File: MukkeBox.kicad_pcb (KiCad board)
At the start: 2 copper layers, 175 x 105 mm, 295 parts, among them J1 TB001-500-06BE CUI_Devices, J101 Conn_02x20_Odd_Even, J103 Conn_02x05_Odd_Even, J104 Conn_02x01, J301 Conn_02x04_Odd_Even, J302 Conn_02x04_Odd_Even, J303 TB001-500-04BE CUI_Devices, J401 TB001-500-02BE CUI_Devices, J601 Conn_01x03_Female, J602 Conn_02x01, J603 Conn_02x06_Odd_Even, J604 Conn_02x01, J605 Conn_02x01, Q1 2N7002, Q201 VS6412AE, Q301 2N7002, Q302 HSBB3103, Q303 2N7002, Q304 HSBB3103, Q305 VS6412AE, Q306 2N7002, Q307 BSS84, Q308 2N7002, Q309 VS6412AE, Q310 HSBB3103, Q311 HSBB3103, Q501 2N7002, U1 TPA3116D2, U102 STM32F030C6Tx_MukkeBox, U103 MCP9700, U2 TPA3116D2, U203 TPS40210, U301 BQ24610, U502 BK8000L, U503 TDA7719, U504 AP2553AW6-7, U505 JW5026, U602 JW5026, Y101 FOXSDLF/080-20

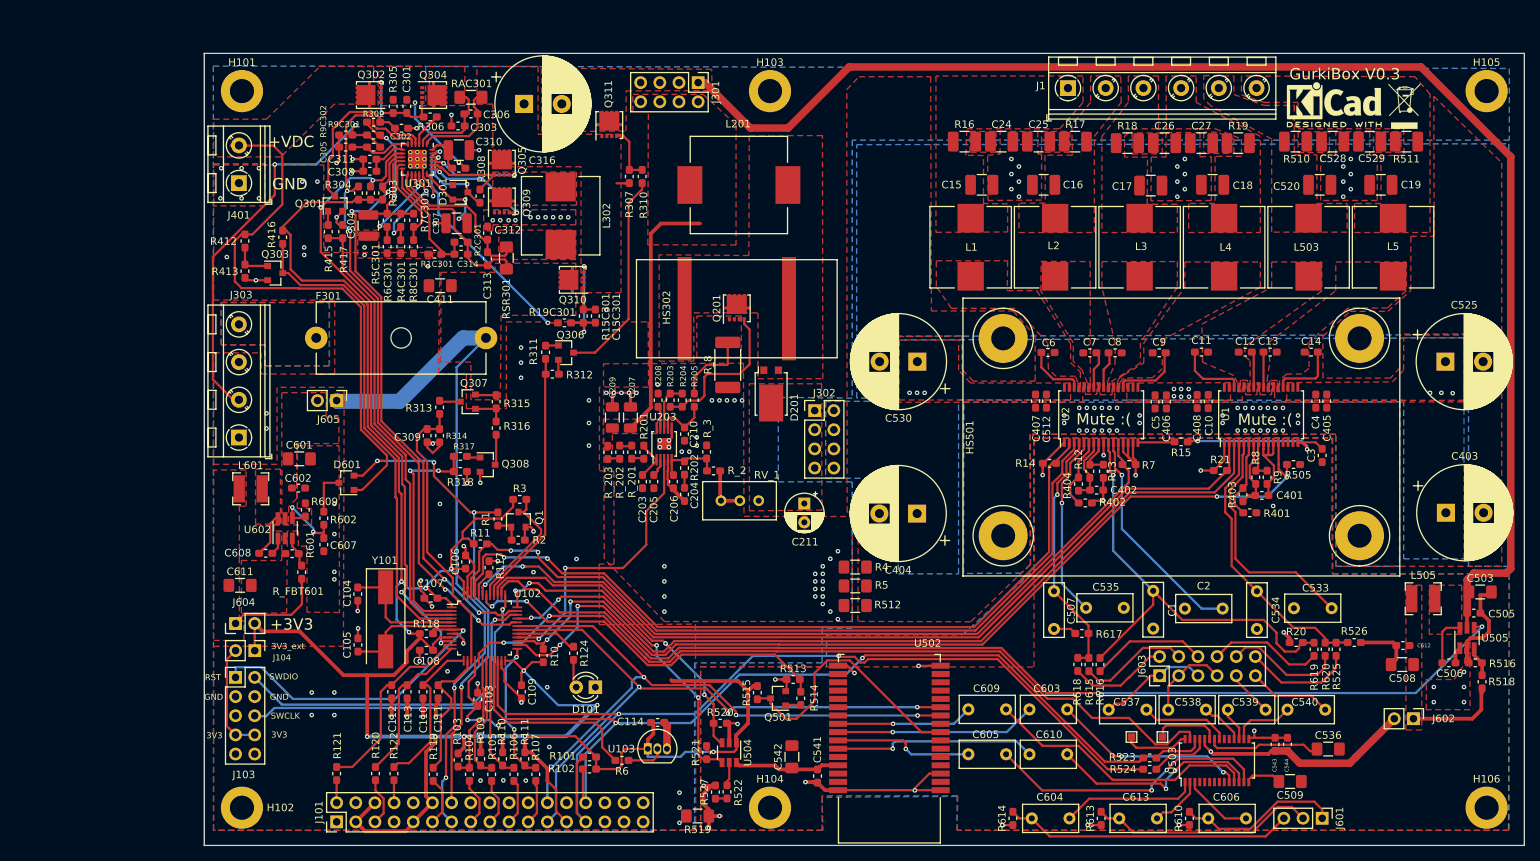
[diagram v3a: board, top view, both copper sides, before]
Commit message: MukkePlatine auf EuroPlatinen groesse geändert
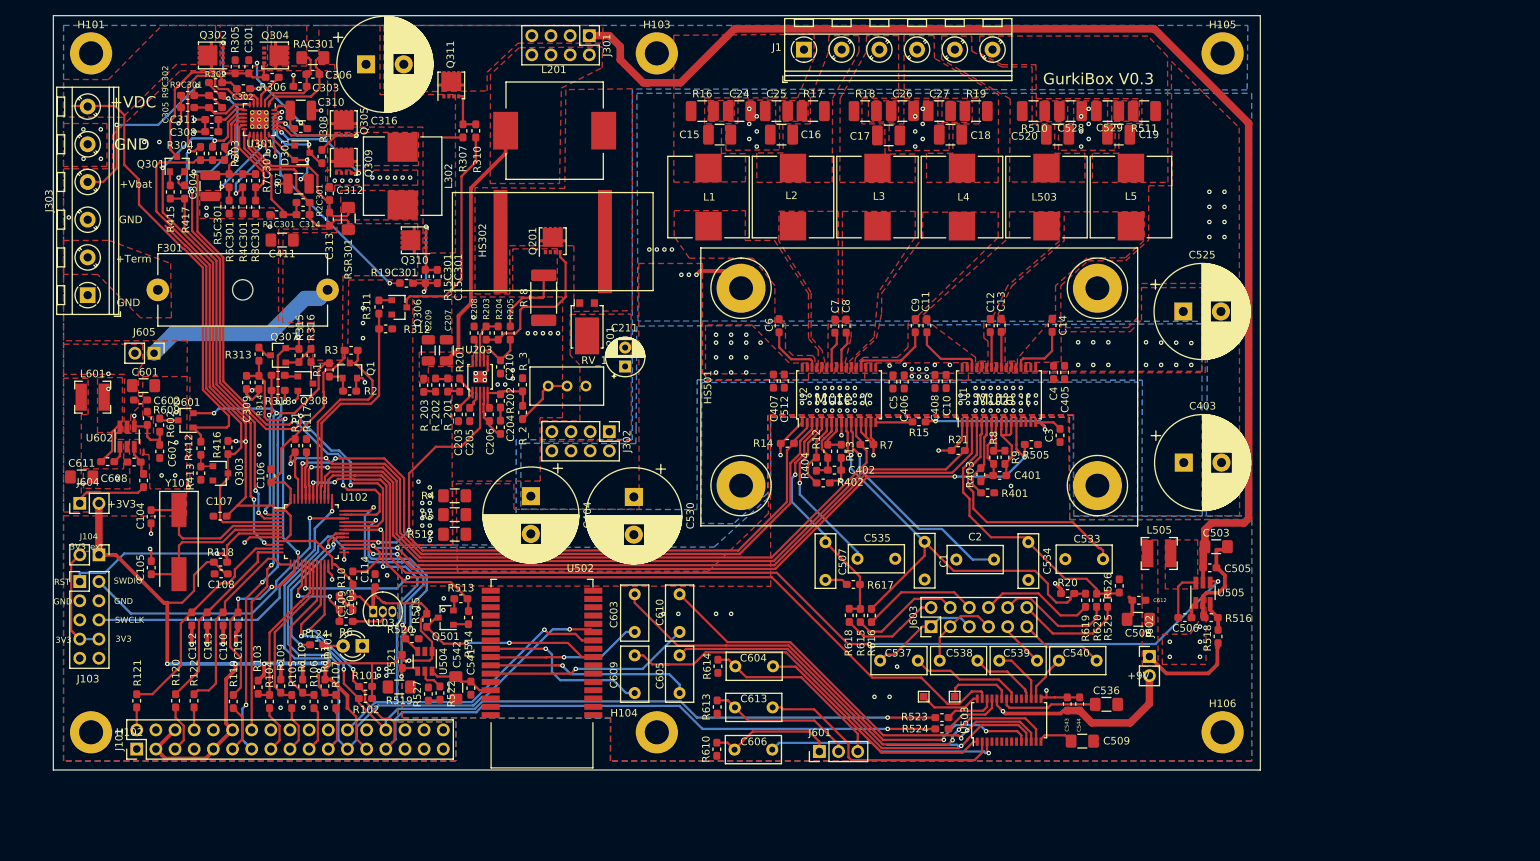
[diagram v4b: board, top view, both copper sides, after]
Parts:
- removed J401: TB001-500-02BE CUI_Devices, TerminalBlock_RND:TerminalBlock_RND_205-00045_1x02_P5.00mm_Horizontal
- removed REF**: WEEE-Logo_4.2x6mm_SilkScreen, Symbol:WEEE-Logo_4.2x6mm_SilkScreen
- removed REF**: KiCad-Logo2_5mm_SilkScreen, Symbol:KiCad-Logo2_5mm_SilkScreen
- J303: value TB001-500-04BE CUI_Devices -> TB001-500-06BE CUI_Devices; footprint TerminalBlock_RND:TerminalBlock_RND_205-00047_1x04_P5.00mm_Horizontal -> TerminalBlock_RND:TerminalBlock_RND_205-00049_1x06_P5.00mm_Horizontal
- moved J601 67.2 mm to (152.0, 129.6), turned to 90 degrees
- moved C606 63.5 mm to (145.8, 129.4)
- moved R610 63.3 mm to (138.4, 129.3)
- moved C603 59.3 mm to (127.5, 108.8), turned to 270 degrees
- moved R4 53.9 mm to (103.7, 95.7)
- moved R5 53.9 mm to (103.7, 98.2)
- moved R512 53.9 mm to (103.7, 100.8)
- moved C613 53.0 mm to (145.8, 123.8)
- moved R613 53.0 mm to (138.5, 123.7)
- moved C404 51.3 mm to (113.8, 95.8), turned to 270 degrees
- moved C610 49.1 mm to (133.5, 113.8), turned to 90 degrees
- moved C541 47.4 mm to (105.8, 121.2)
- moved U502 47.1 mm to (115.2, 119.3)
- moved C542 45.5 mm to (103.8, 121.2), turned to 270 degrees
- moved Q501 45.3 mm to (102.5, 111.9)
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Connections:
- D301 pad 1: (no net) -> Net-(D301-Pad1)
- J101 pad 29: (no net) -> Net-(J101-Pad29)
- J101 pad 30: (no net) -> Net-(J101-Pad30)
- J101 pad 31: (no net) -> Net-(J101-Pad31)
- J101 pad 32: (no net) -> Net-(J101-Pad32)
- J101 pad 33: (no net) -> Net-(J101-Pad33)
- J101 pad 34: (no net) -> Net-(J101-Pad34)
- J103 pad 10: (no net) -> Net-(J103-Pad10)
- J103 pad 5: (no net) -> Net-(J103-Pad5)
- J103 pad 9: (no net) -> Net-(J103-Pad9)
- J303 pad 2: /00_Charger/TS -> Net-(F301-Pad1)
- J303 pad 4: Net-(F301-Pad1) -> /00_Charger/TS
- U502 pad 12: (no net) -> Net-(U502-Pad12)
- U502 pad 13: (no net) -> Net-(U502-Pad13)
- U502 pad 14: (no net) -> Net-(U502-Pad14)
- U502 pad 15: (no net) -> Net-(U502-Pad15)
- U502 pad 18: (no net) -> Net-(U502-Pad18)
- U502 pad 19: (no net) -> Net-(U502-Pad19)
- U502 pad 2: (no net) -> Net-(U502-Pad2)
- U502 pad 20: (no net) -> Net-(U502-Pad20)
- U502 pad 21: (no net) -> Net-(U502-Pad21)
- U502 pad 22: (no net) -> Net-(U502-Pad22)
- U502 pad 23: (no net) -> Net-(U502-Pad23)
- U502 pad 28: (no net) -> Net-(U502-Pad28)
- U502 pad 30: (no net) -> Net-(U502-Pad30)
- U502 pad 31: (no net) -> Net-(U502-Pad31)
- U502 pad 4: (no net) -> Net-(U502-Pad4)
- U502 pad 5: (no net) -> Net-(U502-Pad5)
- U502 pad 6: (no net) -> Net-(U502-Pad6)
- U502 pad 7: (no net) -> Net-(U502-Pad7)
- U502 pad 9: (no net) -> Net-(U502-Pad9)
- U503 pad 19: (no net) -> Net-(U503-Pad19)
- U503 pad 20: (no net) -> Net-(U503-Pad20)
- U503 pad 4: (no net) -> Net-(U503-Pad4)
- U503 pad 5: (no net) -> Net-(U503-Pad5)
- U503 pad 6: (no net) -> Net-(U503-Pad6)
- U503 pad 7: (no net) -> Net-(U503-Pad7)
- U503 pad 8: (no net) -> Net-(U503-Pad8)
- U503 pad 9: (no net) -> Net-(U503-Pad9)
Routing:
- net GNDA: track 112.3 -> 58.3 mm, vias 25 -> 24
- net +3V3: track 321.7 -> 269.8 mm, vias 13 -> 9
- net Net-(C603-Pad1): track 26.0 -> 62.4 mm
- net GND: track 93.2 -> 57.7 mm, vias 119 -> 88
- net Net-(C609-Pad2): track 36.5 -> 71.3 mm, vias 0 -> 1
- net Net-(C610-Pad2): track 28.6 -> 57.4 mm
- net Net-(C613-Pad1): track 7.26 -> 33.6 mm
- net /00_Charger/TS: track 55.4 -> 29.3 mm
- net Net-(C606-Pad1): track 9.27 -> 31.2 mm, vias 0 -> 1
- net MUTE_AMP2: track 126.2 -> 104.3 mm
- net SYSTEM_LOAD: track 185.9 -> 165.1 mm
- net /TEMP_SENSOR1: track 32.7 -> 12.4 mm
- net SDA: track 129.3 -> 109.7 mm, vias 2 -> 3
- net Net-(C605-Pad1): track 37.9 -> 56.9 mm
- net /GPIO4: track 18.7 -> 36.3 mm
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- removed copper zone on B.Cu, net Net-(F301-Pad1)
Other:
- board size 175 x 105 mm -> 160 x 100 mm
- board text added: "+9V"
- board text added: "+Term"
- board text added: "+Vbat"

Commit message: fertig zum bestellen
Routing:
- net Net-(Q201-Pad4): track 20.5 -> 19.4 mm
- net GNDA: vias 24 -> 37
- net GND: vias 88 -> 100

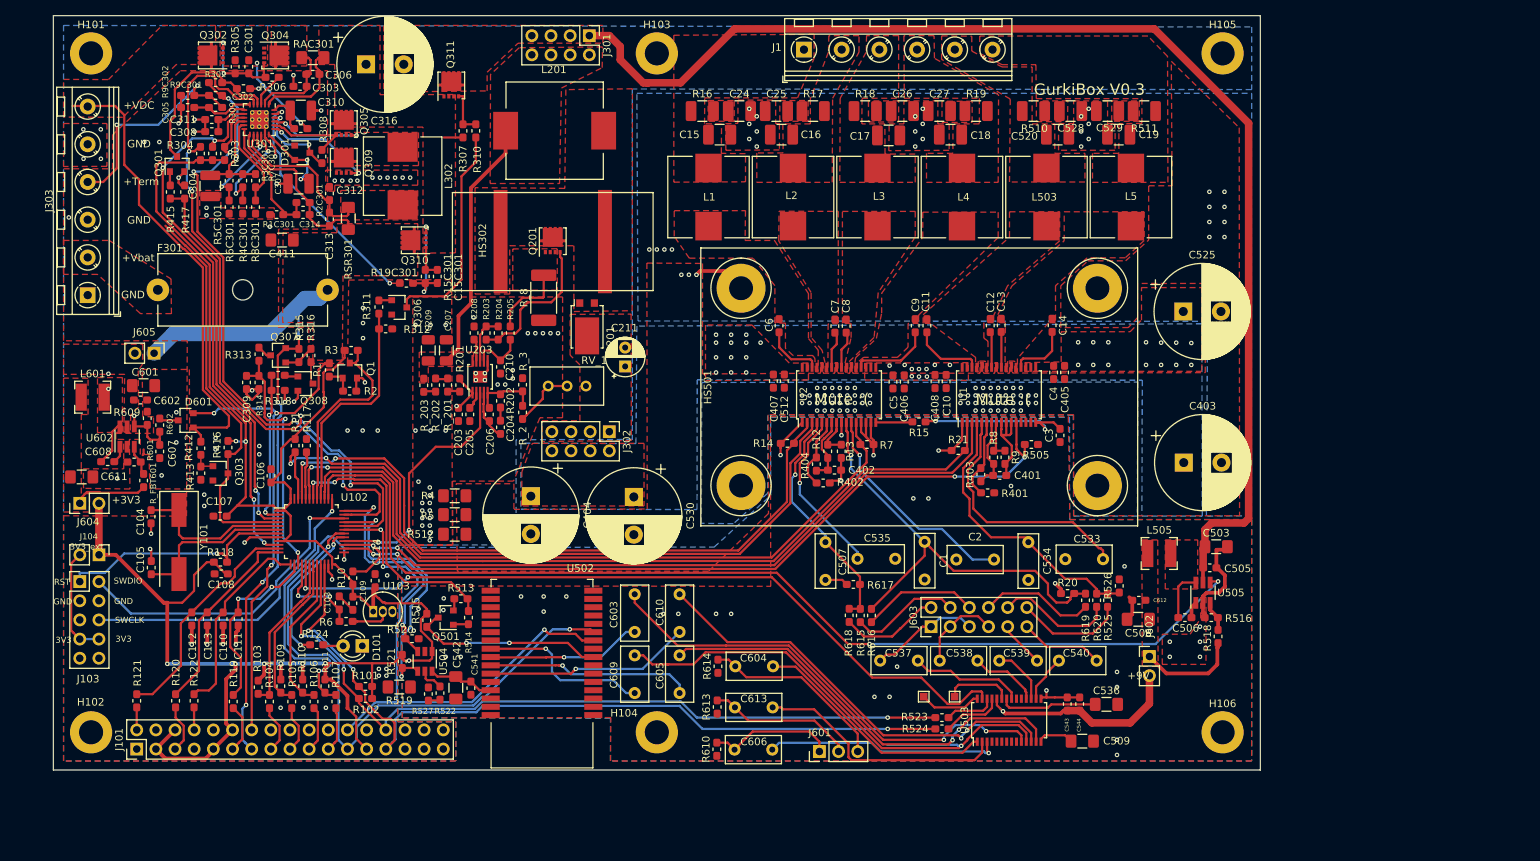
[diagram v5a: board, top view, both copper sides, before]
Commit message: Footprints parallel zu Folienkondensatoren hinzugefügt; Bestellung ist abgeschickt!
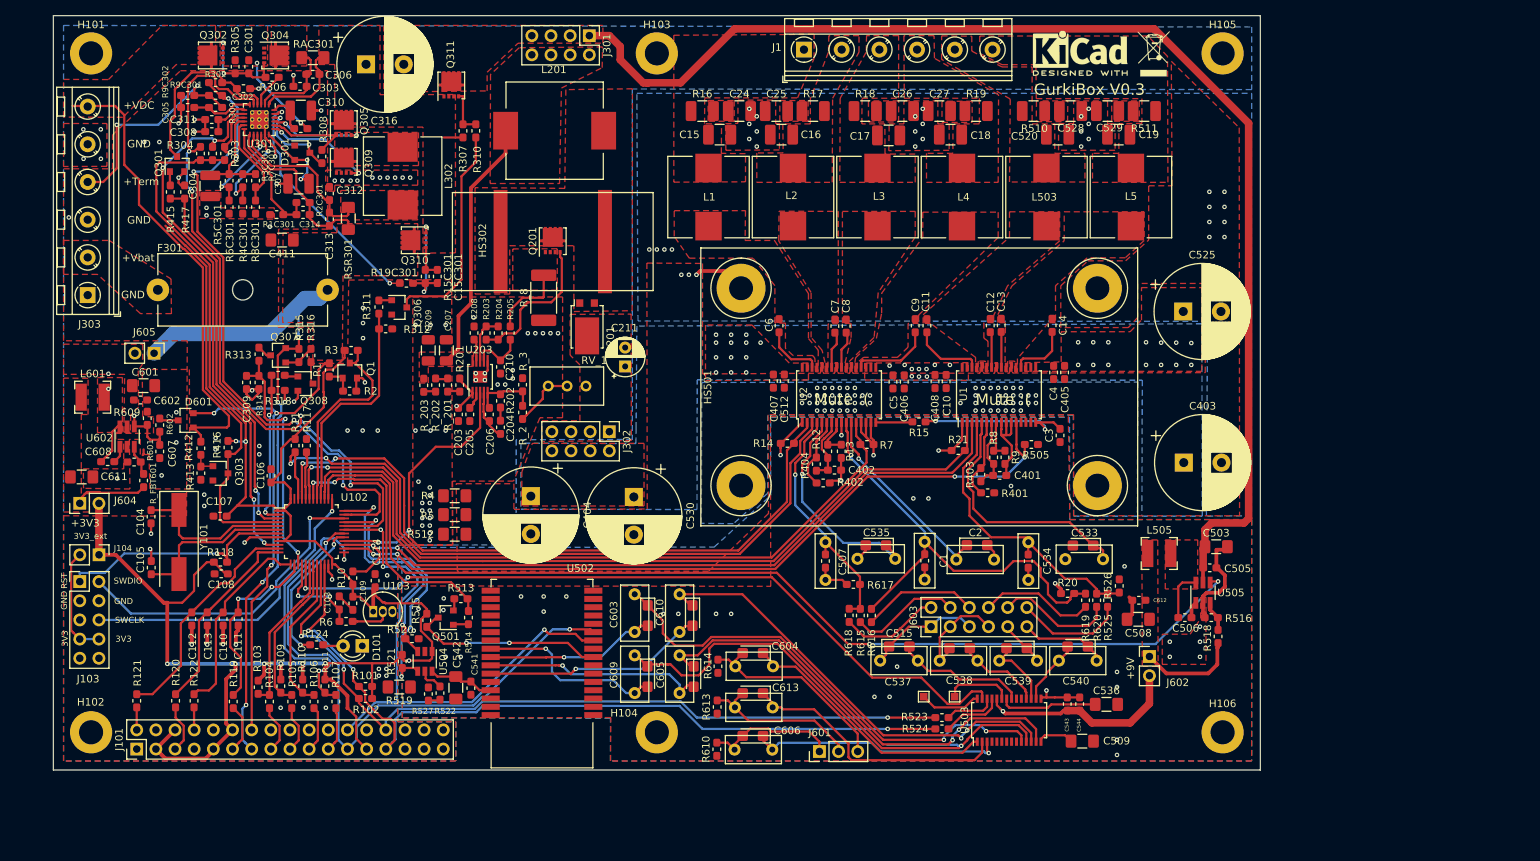
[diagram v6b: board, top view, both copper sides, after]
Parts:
- added C409: 1u DNP, Capacitor_Tantalum_SMD:CP_EIA-3216-18_Kemet-A, F.Cu at (187.0, 102.3)
- added C410: 1u DNP, Capacitor_Tantalum_SMD:CP_EIA-3216-18_Kemet-A, F.Cu at (159.5, 102.3)
- added C412: 1u DNP, Capacitor_Tantalum_SMD:CP_EIA-3216-18_Kemet-A, F.Cu at (172.9, 102.3)
- added C413: 1n DNP, Capacitor_SMD:C_0603_1608Metric_Pad1.05x0.95mm_HandSolder, F.Cu at (166.0, 104.3)
- added C414: 1n DNP, Capacitor_SMD:C_0603_1608Metric_Pad1.05x0.95mm_HandSolder, F.Cu at (152.8, 104.4)
- added C415: 1n DNP, Capacitor_SMD:C_0603_1608Metric_Pad1.05x0.95mm_HandSolder, F.Cu at (179.7, 104.4)
- added C501: 1u DNP, Capacitor_Tantalum_SMD:CP_EIA-3216-18_Kemet-A, F.Cu at (143.2, 116.6)
- added C502: 1u DNP, Capacitor_Tantalum_SMD:CP_EIA-3216-18_Kemet-A, F.Cu at (143.2, 127.6)
- added C504: 1u DNP, Capacitor_Tantalum_SMD:CP_EIA-3216-18_Kemet-A, F.Cu at (143.2, 121.9)
- added C510: 1u DNP, Capacitor_Tantalum_SMD:CP_EIA-3216-18_Kemet-A, F.Cu at (129.3, 111.6)
- added C511: 1u DNP, Capacitor_Tantalum_SMD:CP_EIA-3216-18_Kemet-A, F.Cu at (129.2, 119.7)
- added C513: 1u DNP, Capacitor_Tantalum_SMD:CP_EIA-3216-18_Kemet-A, F.Cu at (135.2, 111.6)
- added C514: 1u DNP, Capacitor_Tantalum_SMD:CP_EIA-3216-18_Kemet-A, F.Cu at (135.3, 119.7)
- added C515: 1u DNP, Capacitor_Tantalum_SMD:CP_EIA-3216-18_Kemet-A, F.Cu at (162.6, 115.7)
- added C516: 1u DNP, Capacitor_Tantalum_SMD:CP_EIA-3216-18_Kemet-A, F.Cu at (170.6, 115.9)
- added C517: 1u DNP, Capacitor_Tantalum_SMD:CP_EIA-3216-18_Kemet-A, F.Cu at (178.2, 115.9)
- added C518: 1u DNP, Capacitor_Tantalum_SMD:CP_EIA-3216-18_Kemet-A, F.Cu at (186.3, 115.7)
- added REF**: WEEE-Logo_4.2x6mm_SilkScreen, Symbol:WEEE-Logo_4.2x6mm_SilkScreen, F.Cu at (196.3, 37.1)
- added REF**: KiCad-Logo2_5mm_SilkScreen, Symbol:KiCad-Logo2_5mm_SilkScreen, F.Cu at (186.6, 37.1)
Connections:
- C2 pad 1: GNDA -> Net-(C2-Pad1)
- C2 pad 2: Net-(C2-Pad2) -> GNDA
- C535 pad 1: GNDA -> Net-(C410-Pad1)
- C535 pad 2: Net-(C535-Pad2) -> GNDA
- D301 pad 1: Net-(D301-Pad1) -> (no net)
- J101 pad 29: Net-(J101-Pad29) -> (no net)
- J101 pad 30: Net-(J101-Pad30) -> (no net)
- J101 pad 31: Net-(J101-Pad31) -> (no net)
- J101 pad 32: Net-(J101-Pad32) -> (no net)
- J101 pad 33: Net-(J101-Pad33) -> (no net)
- J101 pad 34: Net-(J101-Pad34) -> (no net)
- J103 pad 10: Net-(J103-Pad10) -> (no net)
- J103 pad 5: Net-(J103-Pad5) -> (no net)
- J103 pad 9: Net-(J103-Pad9) -> (no net)
- U2 pad 11: Net-(C2-Pad2) -> Net-(C2-Pad1)
- U2 pad 5: Net-(C535-Pad2) -> Net-(C410-Pad1)
- U502 pad 12: Net-(U502-Pad12) -> (no net)
- U502 pad 13: Net-(U502-Pad13) -> (no net)
- U502 pad 14: Net-(U502-Pad14) -> (no net)
- U502 pad 15: Net-(U502-Pad15) -> (no net)
- U502 pad 18: Net-(U502-Pad18) -> (no net)
- U502 pad 19: Net-(U502-Pad19) -> (no net)
- U502 pad 2: Net-(U502-Pad2) -> (no net)
- U502 pad 20: Net-(U502-Pad20) -> (no net)
- U502 pad 21: Net-(U502-Pad21) -> (no net)
- U502 pad 22: Net-(U502-Pad22) -> (no net)
- U502 pad 23: Net-(U502-Pad23) -> (no net)
- U502 pad 28: Net-(U502-Pad28) -> (no net)
- U502 pad 30: Net-(U502-Pad30) -> (no net)
- U502 pad 31: Net-(U502-Pad31) -> (no net)
- U502 pad 4: Net-(U502-Pad4) -> (no net)
- U502 pad 5: Net-(U502-Pad5) -> (no net)
- U502 pad 6: Net-(U502-Pad6) -> (no net)
- U502 pad 7: Net-(U502-Pad7) -> (no net)
- U502 pad 9: Net-(U502-Pad9) -> (no net)
- U503 pad 19: Net-(U503-Pad19) -> (no net)
- U503 pad 20: Net-(U503-Pad20) -> (no net)
- U503 pad 4: Net-(U503-Pad4) -> (no net)
- U503 pad 5: Net-(U503-Pad5) -> (no net)
- U503 pad 6: Net-(U503-Pad6) -> (no net)
- U503 pad 7: Net-(U503-Pad7) -> (no net)
- U503 pad 8: Net-(U503-Pad8) -> (no net)
- U503 pad 9: Net-(U503-Pad9) -> (no net)
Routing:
- net Net-(C2-Pad2): track 29.5 -> 0.00 mm, vias 1 -> 0
- net Net-(C410-Pad1): track 0.00 -> 29.3 mm, vias 0 -> 1
- net Net-(C2-Pad1): track 0.00 -> 26.4 mm, vias 0 -> 1
- net Net-(C535-Pad2): track 22.5 -> 0.00 mm, vias 1 -> 0
- net GNDA: track 58.3 -> 67.6 mm
- net Net-(C511-Pad1): track 71.3 -> 74.7 mm
- net Net-(C514-Pad1): track 56.9 -> 60.2 mm
- net Net-(C504-Pad1): track 33.6 -> 36.0 mm
- net Net-(C513-Pad1): track 57.4 -> 59.7 mm
- net Net-(C518-Pad2): track 6.30 -> 8.64 mm
- net Net-(C515-Pad2): track 15.0 -> 17.3 mm
- net Net-(C502-Pad1): track 31.2 -> 33.5 mm
- net Net-(C516-Pad1): track 11.3 -> 13.6 mm
- net Net-(C501-Pad1): track 32.4 -> 34.7 mm
- net Net-(C504-Pad2): track 19.4 -> 21.7 mm
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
